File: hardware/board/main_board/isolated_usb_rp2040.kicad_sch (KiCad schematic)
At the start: 56 parts, among them J2 Conn_01x03_Male, J4 AudioJack3, J5 USB_C_Receptacle_USB2.0, SW2 SW_DIP_x02, U2 TPD2EUSB30, U3 ADUM4160, U4 RP2040, U5 W25Q16JVUXIQ, X1 ECS-TXO-2016

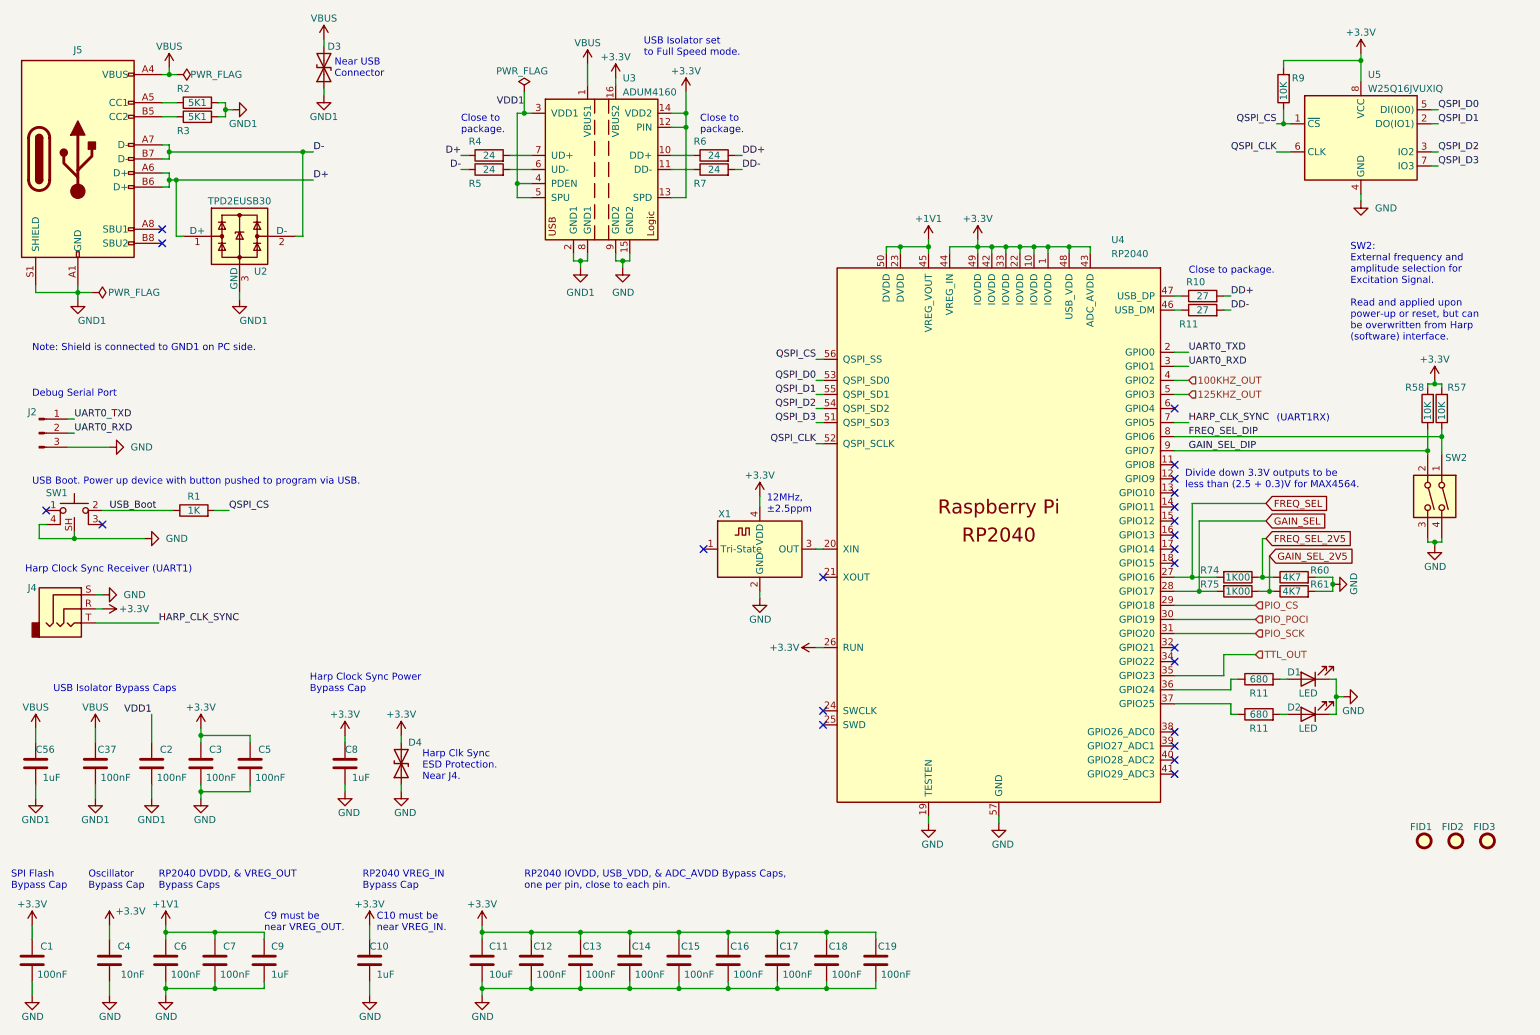
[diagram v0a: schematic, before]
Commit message: split board into two
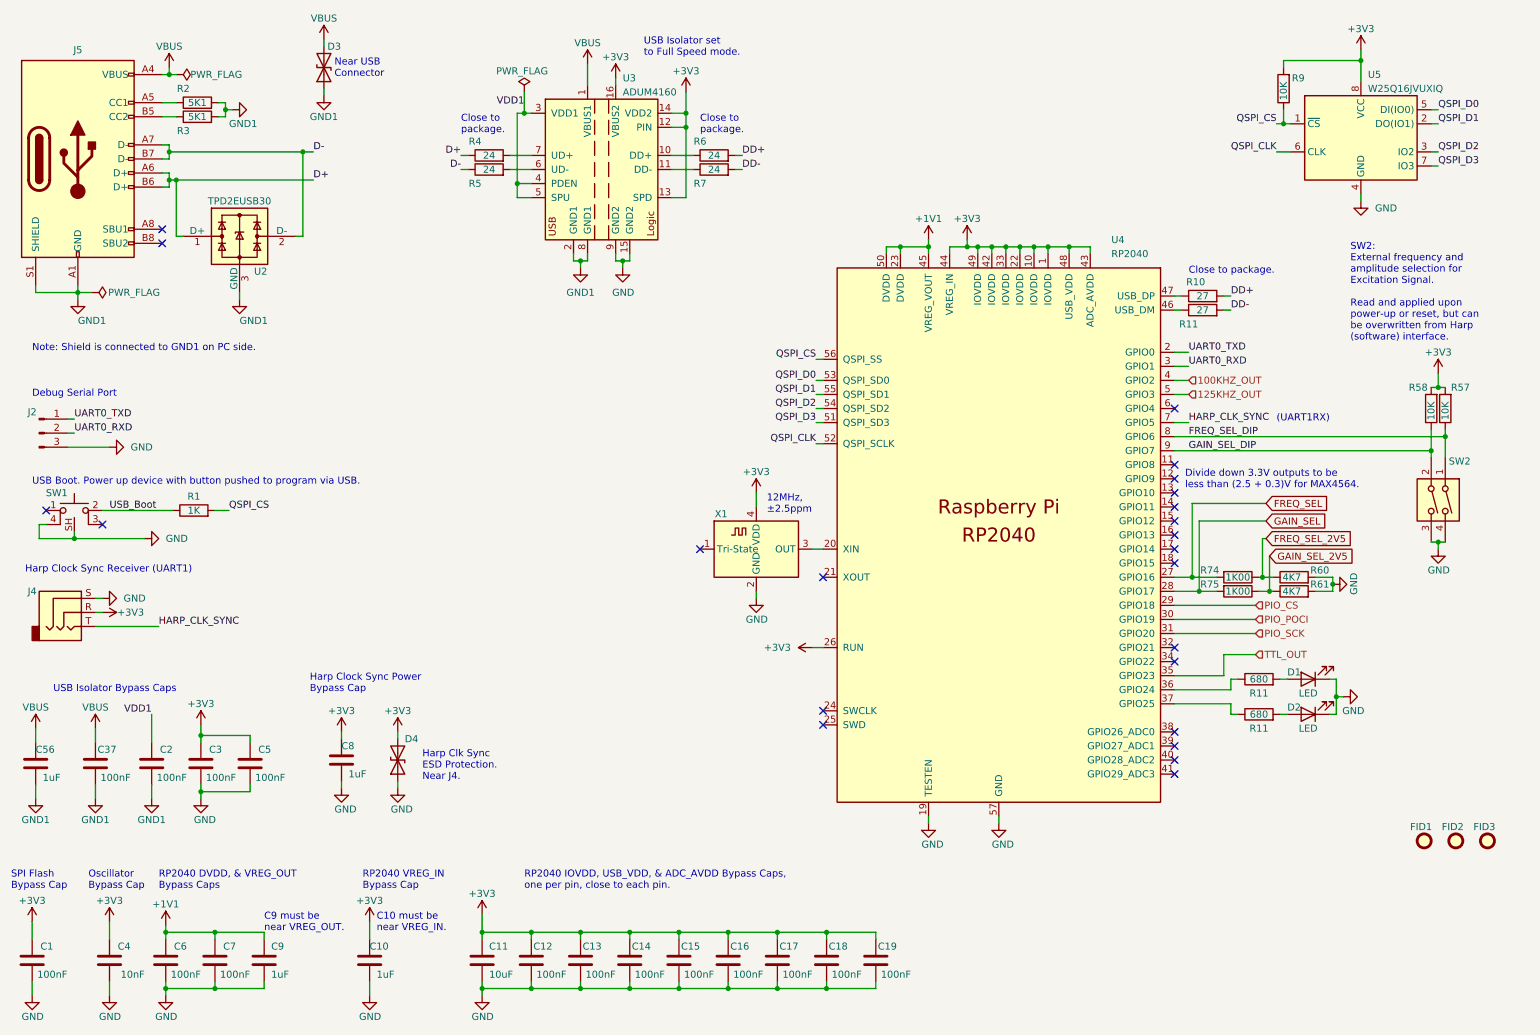
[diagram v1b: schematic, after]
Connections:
- net +3.3V renamed +3V3
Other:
- title: Lickety Split Capacitive Lick Detector -> Lickety Split Capacitive Lick Detector Main Board
- moved on the sheet: C8, D4, J4, R57, R58, SW2, X1

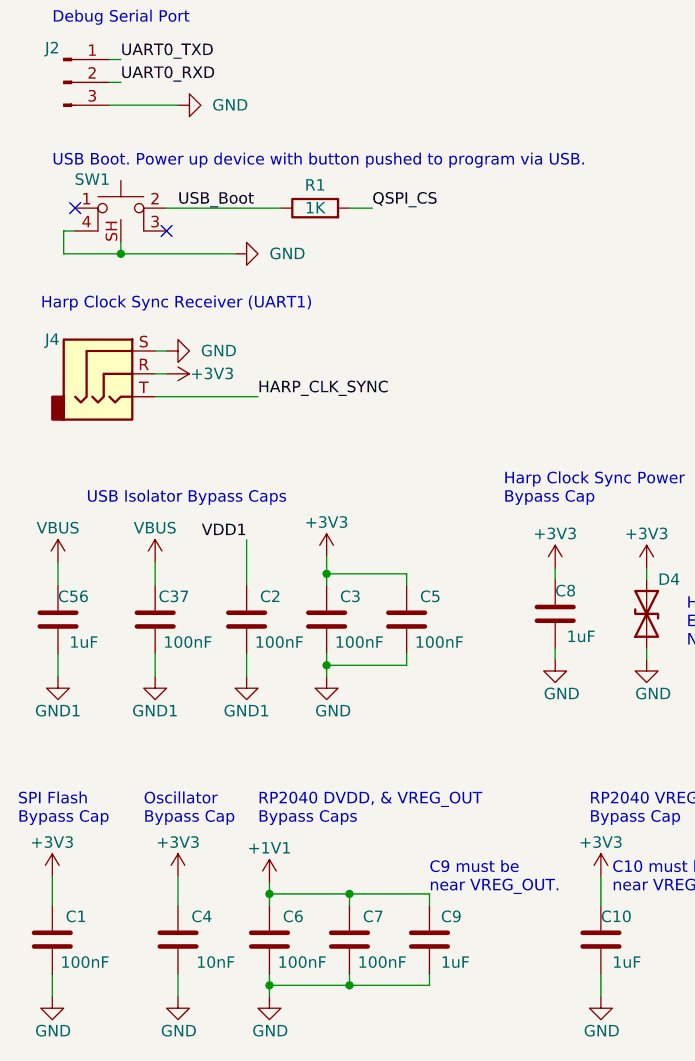
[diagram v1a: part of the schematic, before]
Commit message: update buffer board soldermask cutout
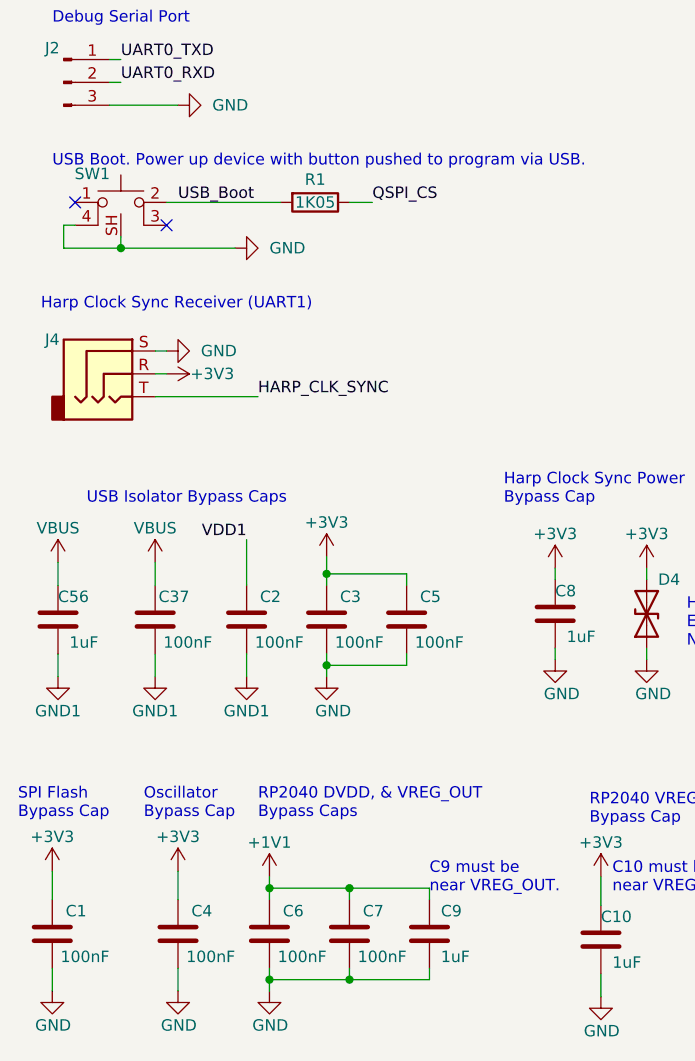
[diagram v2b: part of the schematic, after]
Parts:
- C11: Alternate CL21B106KOQNNNE -> (none)
- C4: value 10nF -> 100nF; Link https://www.digikey.com/en/products/detail/yageo/CC0402KPX7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 -> https://www.digikey.com/en/products/detail/walsin-technolog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; Manufacturer Yageo -> Walson Technology Corporation; Manufacturer Number CC0402KPX7R8BB103 -> 0402B104K160CT; PCBWay Link (none) -> https://www.pcbway.com/components/detail/0402B104K160CT/307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; Rated Voltage 25V -> 16V
- D3: Alternate PESD5V0F1BLD,315 -> (none); Link https://www.digikey.com/en/products/detail/onsemi/ESD7571N2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 -> https://www.digikey.com/en/products/detail/nexperia-usa-inc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; Manufacturer onsemi -> Nexperia USA Inc.; Manufacturer Number ESD7571N2T5G -> PESD5V0F1BLD,315
- D4: Link https://www.digikey.com/en/products/detail/onsemi/ESD7571N2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 -> https://www.digikey.com/en/products/detail/nexperia-usa-inc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; Manufacturer onsemi -> Nexperia USA Inc.; Manufacturer Number ESD7571N2T5G -> PESD5V0F1BLD,315
- R1: value 1K -> 1K05; Link https://www.digikey.com/en/products/detail/yageo/RT0402BRD071KL/1069118 -> https://www.digikey.com/en/products/detail/yageo/RT0402BRD071K05L/1069088; Manufacturer Number RT0402BRD071KL -> RT0402BRD071K05L; Tolerance 1% -> 0.1%
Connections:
- net QSPI_CS: now also R1.1; no longer R1.2
- net USB_Boot: now also R1.2; no longer R1.1
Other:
- moved on the sheet: C1, C6, C7, C9, SW1
